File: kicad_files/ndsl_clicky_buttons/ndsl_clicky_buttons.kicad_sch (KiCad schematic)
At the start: 13 parts, among them SW1 UP, SW2 LEFT, SW3 DOWN, SW4 RIGHT

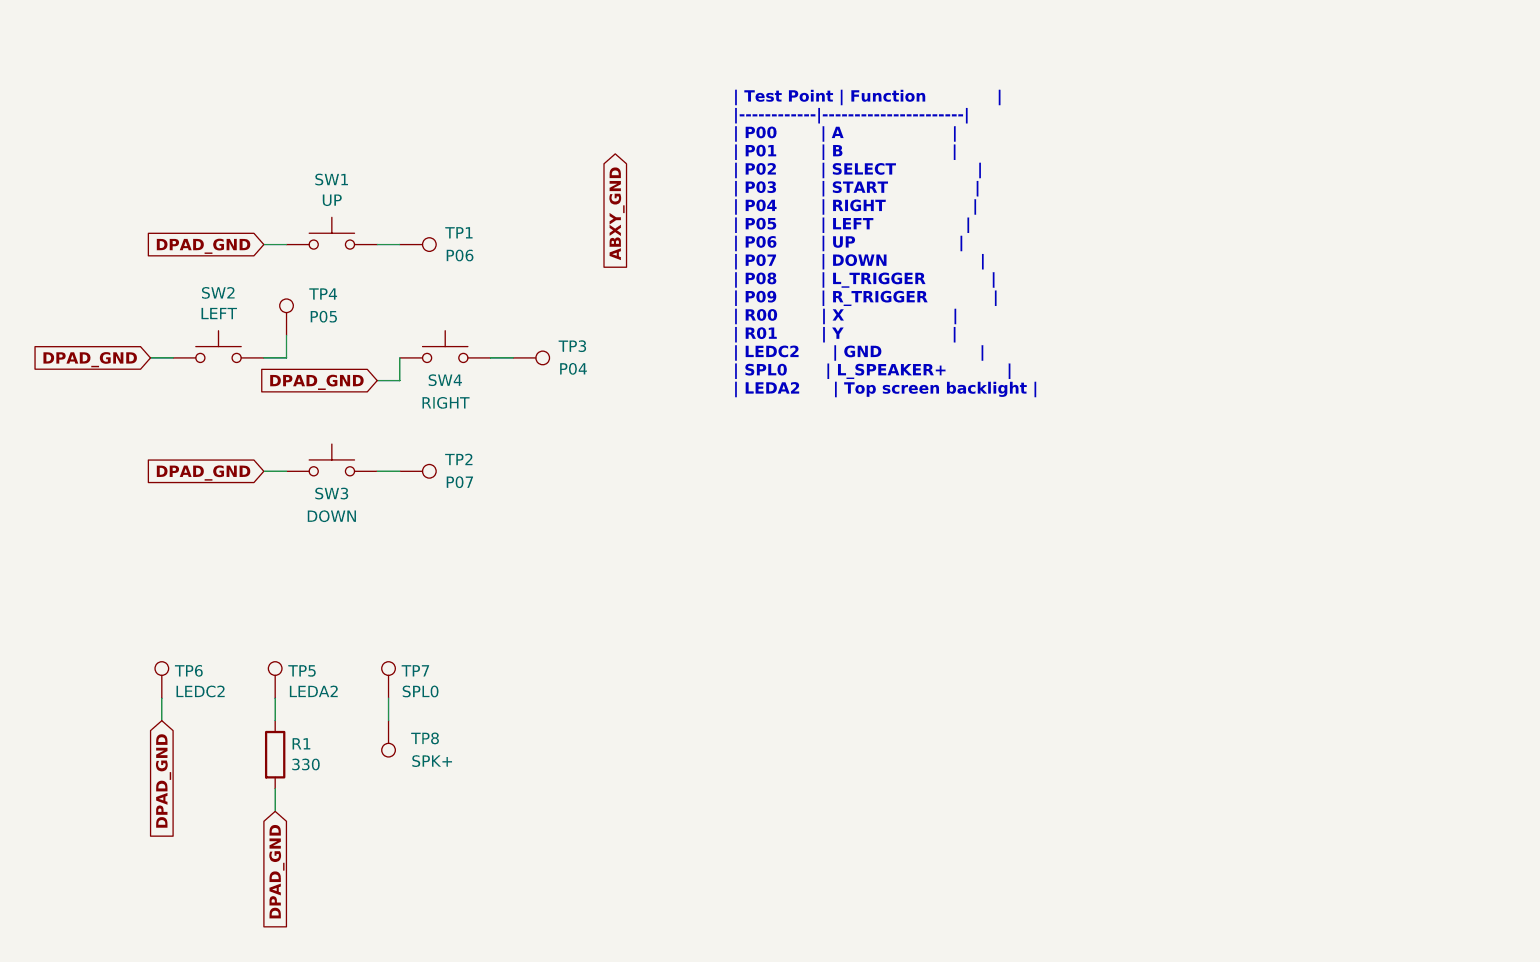
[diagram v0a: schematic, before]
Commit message: Add custom test point footprint
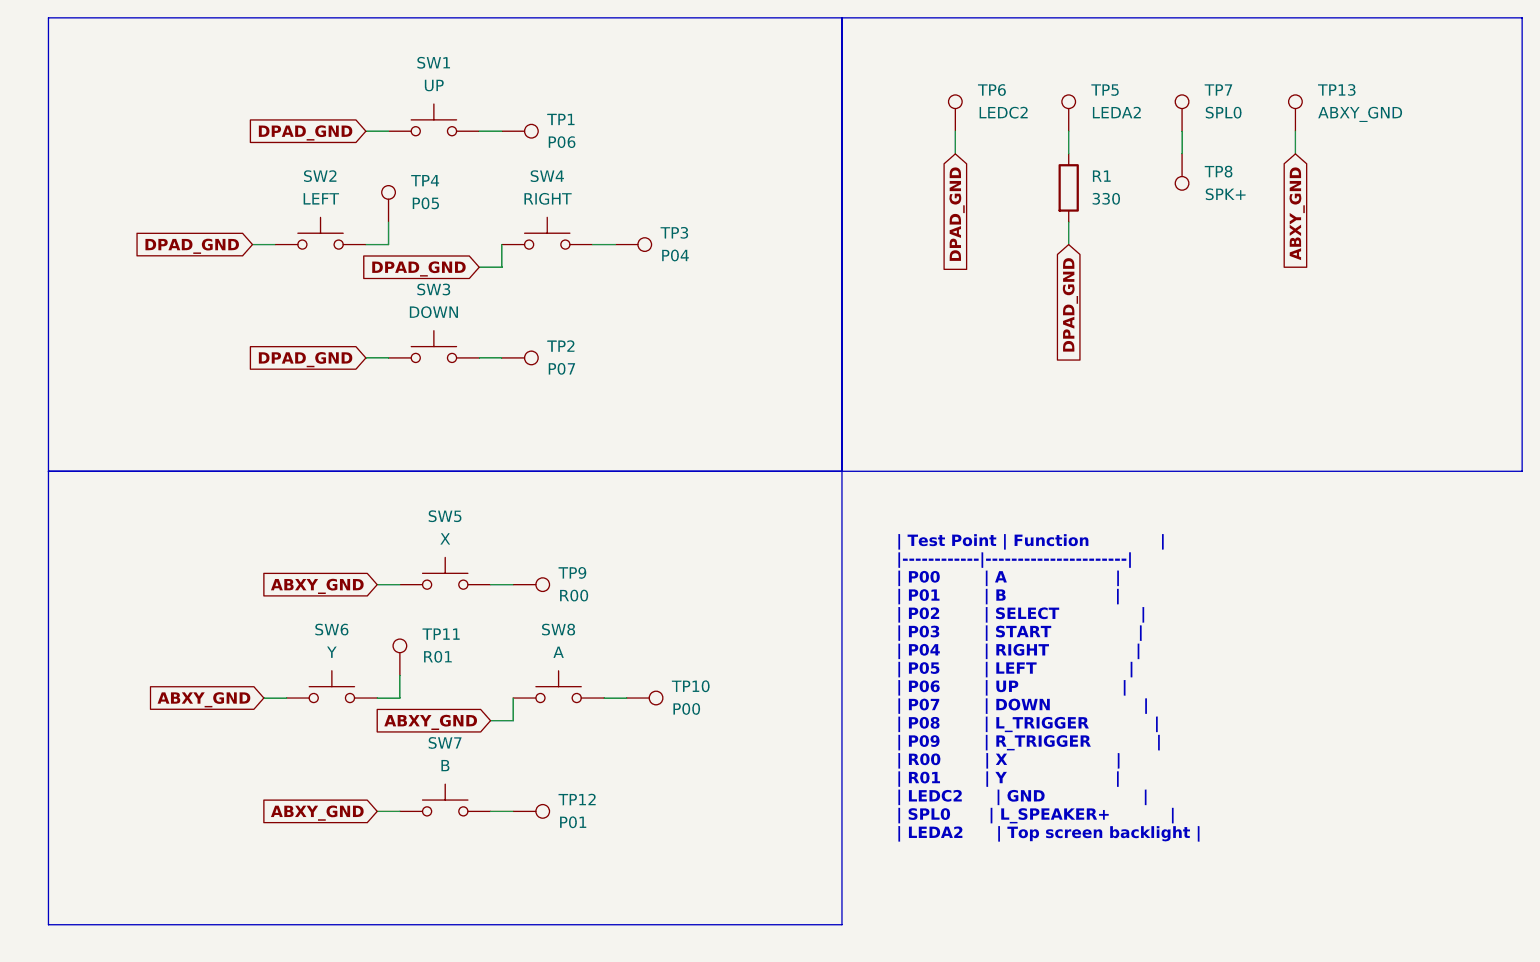
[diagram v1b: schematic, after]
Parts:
- added SW5: X, symbol Switch:SW_Push
- added SW6: Y, symbol Switch:SW_Push
- added SW7: B, symbol Switch:SW_Push
- added SW8: A, symbol Switch:SW_Push
- added TP10: P00, ndsl_clicky_buttons:TestPoint_THTPad_D1.5mm_Drill1.0mm, symbol Connector:TestPoint
- added TP11: R01, ndsl_clicky_buttons:TestPoint_THTPad_D1.5mm_Drill1.0mm, symbol Connector:TestPoint
- added TP12: P01, ndsl_clicky_buttons:TestPoint_THTPad_D1.5mm_Drill1.0mm, symbol Connector:TestPoint
- added TP13: ABXY_GND, symbol Connector:TestPoint
- added TP9: R00, ndsl_clicky_buttons:TestPoint_THTPad_D1.5mm_Drill1.0mm, symbol Connector:TestPoint
- TP1, TP2, TP3, TP4, TP5, TP6, TP7: footprint custom_connectors:1mm_test_point -> ndsl_clicky_buttons:TestPoint_THTPad_D1.5mm_Drill1.0mm
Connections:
- net ABXY_GND: now also SW5.1, SW6.1, SW7.1, SW8.1, TP13.1
- new net: SW6.2, TP11.1
- new net: SW5.2, TP9.1
- new net: SW7.2, TP12.1
- new net: SW8.2, TP10.1
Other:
- moved on the sheet: R1, SW1, SW2, SW3, SW4, TP1, TP2, TP3, TP4, TP5, TP6, TP7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

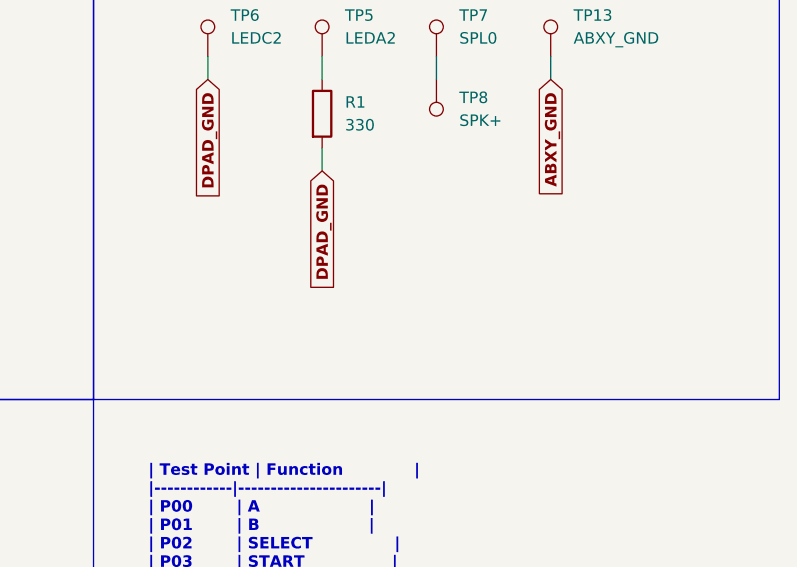
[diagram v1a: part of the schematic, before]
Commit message: Add solder jumper to enable Macro screen bypass
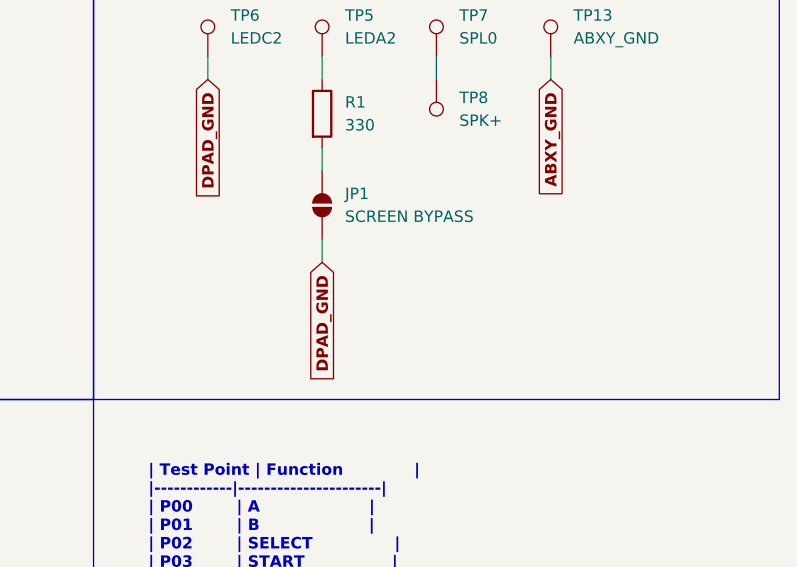
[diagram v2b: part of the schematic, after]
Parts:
- added JP1: SCREEN BYPASS, Jumper:SolderJumper-2_P1.3mm_Open_RoundedPad1.0x1.5mm, symbol Jumper:SolderJumper_2_Open
- SW1, SW2, SW3, SW4: footprint buttons_custom:gba_sp_buttons -> ndsl_clicky_buttons:ALPS_SKRR
- SW5, SW6, SW7, SW8: footprint (none) -> ndsl_clicky_buttons:ALPS_SKRR
- TP13: footprint (none) -> ndsl_clicky_buttons:TestPoint_THTPad_D1.5mm_Drill1.0mm
- TP8: footprint custom_connectors:2mm_test_point_smd -> TestPoint:TestPoint_Pad_2.0x2.0mm
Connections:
- net DPAD_GND: now also JP1.1 (A); no longer R1.2
- new net: JP1.2 (B), R1.2
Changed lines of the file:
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@@
+	(wire
+		(pts
+			(xy 127 45.72) (xy 127 48.26)
+		)
+		(stroke
+			(width 0)
+			(type default)
+		)
+	)
 	(wire
 		(pts
@@
 	(global_label "DPAD_GND"
 		(shape input)
-		(at 127 38.1 270)
+		(at 127 48.26 270)
 		(fields_autoplaced yes)
 		(effects
@@
 		)
 		(property "Intersheetrefs" "${INTERSHEET_REFS}"
-			(at 127 50.6437 90)
+			(at 127 60.8037 90)
 			(effects
 				(font
@@
 			)
 		)
-		(property "Footprint" "buttons_custom:gba_sp_buttons"
+		(property "Footprint" "ndsl_clicky_buttons:ALPS_SKRR"
 			(at 55.88 20.32 0)
 			(effects
@@
 			)
 		)
-		(property "Footprint" "buttons_custom:gba_sp_buttons"
+		(property "Footprint" "ndsl_clicky_buttons:ALPS_SKRR"
 			(at 55.88 45.72 0)
 			(effects
@@
 			)
 		)
-		(property "Footprint" "buttons_custom:gba_sp_buttons"
+		(property "Footprint" "ndsl_clicky_buttons:ALPS_SKRR"
 			(at 43.18 33.02 0)
 			(effects
@@
 			)
 		)
-		(property "Footprint" "buttons_custom:gba_sp_buttons"
+		(property "Footprint" "ndsl_clicky_buttons:ALPS_SKRR"
 			(at 68.58 33.02 0)
 			(effects
@@
 			)
 		)
-		(property "Footprint" "custom_connectors:2mm_test_point_smd"
+		(property "Footprint" "TestPoint:TestPoint_Pad_2.0x2.0mm"
 			(at 134.62 27.94 0)
 			(effects
@@
 			)
 		)
-		(property "Footprint" ""
+		(property "Footprint" "ndsl_clicky_buttons:TestPoint_THTPad_D1.5mm_Drill1.0mm"
 			(at 157.48 25.4 0)
 			(effects
@@
 	)
 	(symbol
+		(lib_id "Jumper:SolderJumper_2_Open")
+		(at 127 41.91 90)
+		(unit 1)
+		(exclude_from_sim no)
+		(in_bom no)
+		(on_board yes)
+		(dnp no)
+		(fields_autoplaced yes)
+		(property "Reference" "JP1"
+			(at 129.54 40.6399 90)
+			(effects
+				(font
+					(size 1.27 1.27)
+				)
+				(justify right)
+			)
+		)
+		(property "Value" "SCREEN BYPASS"
+			(at 129.54 43.1799 90)
+			(effects
+				(font
+					(size 1.27 1.27)
+				)
+				(justify right)
+			)
+		)
+		(property "Footprint" "Jumper:SolderJumper-2_P1.3mm_Open_RoundedPad1.0x1.5mm"
+			(at 127 41.91 0)
+			(effects
+				(font
+					(size 1.27 1.27)
+				)
+				(hide yes)
+			)
+		)
+		(property "Datasheet" "~"
+			(at 127 41.91 0)
+			(effects
+				(font
+					(size 1.27 1.27)
+				)
+				(hide yes)
+			)
+		)
+		(property "Description" "Solder Jumper, 2-pole, open"
+			(at 127 41.91 0)
+			(effects
+				(font
+					(size 1.27 1.27)
+				)
+				(hide yes)
+			)
+		)
+		(pin "1"
+		)
+		(pin "2"
+		)
+		(instances
+			(project ""
+				(path "/2de16c95-9e2c-4937-bd2d-06213c9bc92f"
+					(reference "JP1")
+					(unit 1)
+				)
+			)
+		)
+	)
+	(symbol
 		(lib_id "Switch:SW_Push")
 		(at 44.45 88.9 0)
@@
 			)
 		)
-		(property "Footprint" ""
+		(property "Footprint" "ndsl_clicky_buttons:ALPS_SKRR"
 			(at 44.45 83.82 0)
 			(effects
@@
 			)
 		)
-		(property "Footprint" ""
+		(property "Footprint" "ndsl_clicky_buttons:ALPS_SKRR"
 			(at 57.15 71.12 0)
 			(effects
@@
 			)
 		)
-		(property "Footprint" ""
+		(property "Footprint" "ndsl_clicky_buttons:ALPS_SKRR"
 			(at 57.15 96.52 0)
 			(effects
@@
 			)
 		)
-		(property "Footprint" ""
+		(property "Footprint" "ndsl_clicky_buttons:ALPS_SKRR"
 			(at 69.85 83.82 0)
 			(effects

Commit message: Put both boards together
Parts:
- TP13: footprint ndsl_clicky_buttons:TestPoint_THTPad_D1.5mm_Drill1.0mm -> TestPoint:TestPoint_Pad_2.0x2.0mm
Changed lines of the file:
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@@
 			)
 		)
-		(property "Footprint" "ndsl_clicky_buttons:TestPoint_THTPad_D1.5mm_Drill1.0mm"
+		(property "Footprint" "TestPoint:TestPoint_Pad_2.0x2.0mm"
 			(at 157.48 25.4 0)
 			(effects
